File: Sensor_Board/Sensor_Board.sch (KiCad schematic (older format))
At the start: 15 parts, among them J1 Mic_Conn, U1 TLV741PxxDQNx

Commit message: Start board layout
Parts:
- removed U1: TLV741PxxDQNx, grootvoet:Texas_X2SON-4_1x1mm_P0.65mm, symbol grootvoet:TLV741PxxDQNx
- added D1: RED, LED_SMD:LED_0603_1608Metric_Pad1.05x0.95mm_HandSolder, symbol Device:LED_Small
- added R21: 2k2, Resistor_SMD:R_0603_1608Metric_Pad0.98x0.95mm_HandSolder, symbol Device:R_Small
- added U1: TLV741PxxDBVx, Package_TO_SOT_SMD:SOT-23-5, symbol grootvoet:TLV741PxxDBVx
- H1, H2: footprint MountingHole:MountingHole_2.7mm_M2.5_DIN965_Pad -> MountingHole:MountingHole_3.2mm_M3_Pad_Via
- J1: footprint Connector_PinHeader_2.54mm:PinHeader_1x08_P2.54mm_Vertical -> Connector_PinHeader_2.00mm:PinHeader_1x08_P2.00mm_Vertical
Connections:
- net +1V8: now also U1.5 (OUT)
- net +3V3: now also U1.1 (IN)
- net EN: now also U1.3 (EN)
- net GND: now also R21.2, U1.2 (GND)
- net VCC: now also D1.2 (A)
- new net: D1.1 (K), R21.1
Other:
- moved on the sheet: CB2, H1, H2, J1, R1
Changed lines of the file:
@@
 L Connector_Generic:Conn_01x08 J?
 U 1 1 5F9760C7
-P 5800 4200
+P 4650 4050
 AR Path="/5F1E182A/5F9760C7" Ref="J?"  Part="1"
 AR Path="/5EE5ECAD/5EE62C2B/5F9760C7" Ref="J?"  Part="1"
@@
 AR Path="/5F803BE9/5F9760C7" Ref="J?"  Part="1"
 AR Path="/5F9760C7" Ref="J1"  Part="1"
-F 0 "J1" H 5800 3600 50  0000 C CNN
-F 1 "Mic_Conn" H 5800 3700 50  0000 C CNN
-F 2 "Connector_PinHeader_2.54mm:PinHeader_1x08_P2.54mm_Vertical" H 5800 4200 50  0001 C CNN
-F 3 "~" H 5800 4200 50  0001 C CNN
-F 4 "" H 5800 4200 50  0001 C CNN "MPN"
-F 5 "" H 5800 4200 50  0001 C CNN "Mfr."
-	1    5800 4200
+F 0 "J1" H 4650 3450 50  0000 C CNN
+F 1 "Mic_Conn" H 4650 3550 50  0000 C CNN
+F 2 "Connector_PinHeader_2.00mm:PinHeader_1x08_P2.00mm_Vertical" H 4650 4050 50  0001 C CNN
+F 3 "~" H 4650 4050 50  0001 C CNN
+F 4 "" H 4650 4050 50  0001 C CNN "MPN"
+F 5 "" H 4650 4050 50  0001 C CNN "Mfr."
+	1    4650 4050
 	1    0    0    1
 $EndComp
@@
 L Device:R_Small R?
 U 1 1 5F976175
-P 4150 4100
+P 3750 4000
 AR Path="/5EE5ECAD/5EECE6B8/5F976175" Ref="R?"  Part="1"
 AR Path="/5EE5ECAD/5EF21991/5F976175" Ref="R?"  Part="1"
@@
 AR Path="/5F803BE9/5F976175" Ref="R?"  Part="1"
 AR Path="/5F976175" Ref="R1"  Part="1"
-F 0 "R1" H 4209 4146 50  0000 L CNN
-F 1 "100k" H 4209 4055 50  0000 L CNN
-F 2 "Resistor_SMD:R_0603_1608Metric_Pad0.98x0.95mm_HandSolder" H 4150 4100 50  0001 C CNN
-F 3 "~" H 4150 4100 50  0001 C CNN
-F 4 "RC0603FR-07100KL" H 4150 4100 50  0001 C CNN "MPN"
-F 5 "Yageo" H 4150 4100 50  0001 C CNN "Mfr."
-	1    4150 4100
+F 0 "R1" H 3809 4046 50  0000 L CNN
+F 1 "100k" H 3809 3955 50  0000 L CNN
+F 2 "Resistor_SMD:R_0603_1608Metric_Pad0.98x0.95mm_HandSolder" H 3750 4000 50  0001 C CNN
+F 3 "~" H 3750 4000 50  0001 C CNN
+F 4 "RC0603FR-07100KL" H 3750 4000 50  0001 C CNN "MPN"
+F 5 "Yageo" H 3750 4000 50  0001 C CNN "Mfr."
+	1    3750 4000
 	1    0    0    -1
 $EndComp
@@
 L Device:C_Small CB?
 U 1 1 5F976195
-P 3650 4100
+P 3250 4000
 AR Path="/5EE5ECAD/5EECE6B8/5F976195" Ref="CB?"  Part="1"
 AR Path="/5EE5ECAD/5EF21991/5F976195" Ref="CB?"  Part="1"
@@
 AR Path="/5F803BE9/5F976195" Ref="CB?"  Part="1"
 AR Path="/5F976195" Ref="CB2"  Part="1"
-F 0 "CB2" H 3742 4146 50  0000 L CNN
-F 1 "100n" H 3742 4055 50  0000 L CNN
-F 2 "Capacitor_SMD:C_0603_1608Metric_Pad1.08x0.95mm_HandSolder" H 3650 4100 50  0001 C CNN
-F 3 "~" H 3650 4100 50  0001 C CNN
-F 4 "C0603C104M5RACTU" H 3650 4100 50  0001 C CNN "MPN"
-F 5 "KEMET" H 3650 4100 50  0001 C CNN "Mfr."
-	1    3650 4100
+F 0 "CB2" H 3342 4046 50  0000 L CNN
+F 1 "100n" H 3342 3955 50  0000 L CNN
+F 2 "Capacitor_SMD:C_0603_1608Metric_Pad1.08x0.95mm_HandSolder" H 3250 4000 50  0001 C CNN
+F 3 "~" H 3250 4000 50  0001 C CNN
+F 4 "C0603C104M5RACTU" H 3250 4000 50  0001 C CNN "MPN"
+F 5 "KEMET" H 3250 4000 50  0001 C CNN "Mfr."
+	1    3250 4000
 	1    0    0    -1
 $EndComp
@@
 L Mechanical:MountingHole H?
 U 1 1 5F9761A0
-P 6500 3750
+P 6500 3800
 AR Path="/5EE5ECAD/5EECE6B8/5F9761A0" Ref="H?"  Part="1"
 AR Path="/5EE5ECAD/5EF4C631/5F9761A0" Ref="H?"  Part="1"
@@
 AR Path="/5F803BE9/5F9761A0" Ref="H?"  Part="1"
 AR Path="/5F9761A0" Ref="H2"  Part="1"
-F 0 "H2" H 6600 3796 50  0000 L CNN
-F 1 "MountingHole" H 6600 3705 50  0000 L CNN
-F 2 "MountingHole:MountingHole_2.7mm_M2.5_DIN965_Pad" H 6500 3750 50  0001 C CNN
-F 3 "~" H 6500 3750 50  0001 C CNN
-	1    6500 3750
+F 0 "H2" H 6600 3846 50  0000 L CNN
+F 1 "MountingHole" H 6600 3755 50  0000 L CNN
+F 2 "MountingHole:MountingHole_3.2mm_M3_Pad_Via" H 6500 3800 50  0001 C CNN
+F 3 "~" H 6500 3800 50  0001 C CNN
+	1    6500 3800
 	1    0    0    -1
 $EndComp
@@
 L Mechanical:MountingHole H?
 U 1 1 5F9761A6
-P 6500 3550
+P 6500 3600
 AR Path="/5EE5ECAD/5EECE6B8/5F9761A6" Ref="H?"  Part="1"
 AR Path="/5EE5ECAD/5EF4C631/5F9761A6" Ref="H?"  Part="1"
@@
 AR Path="/5F803BE9/5F9761A6" Ref="H?"  Part="1"
 AR Path="/5F9761A6" Ref="H1"  Part="1"
-F 0 "H1" H 6600 3596 50  0000 L CNN
-F 1 "MountingHole" H 6600 3505 50  0000 L CNN
-F 2 "MountingHole:MountingHole_2.7mm_M2.5_DIN965_Pad" H 6500 3550 50  0001 C CNN
-F 3 "~" H 6500 3550 50  0001 C CNN
-	1    6500 3550
+F 0 "H1" H 6600 3646 50  0000 L CNN
+F 1 "MountingHole" H 6600 3555 50  0000 L CNN
+F 2 "MountingHole:MountingHole_3.2mm_M3_Pad_Via" H 6500 3600 50  0001 C CNN
+F 3 "~" H 6500 3600 50  0001 C CNN
+	1    6500 3600
 	1    0    0    -1
 $EndComp
@@
 F 5 "KEMET" H 6300 5400 50  0001 C CNN "Mfr."
 	1    6300 5400
-	1    0    0    -1
-$EndComp
-$Comp
-L grootvoet:TLV741PxxDQNx U1
-U 1 1 5F9A84F9
-P 4250 5300
-F 0 "U1" H 4275 5665 50  0000 C CNN
-F 1 "TLV741PxxDQNx" H 4275 5574 50  0000 C CNN
-F 2 "grootvoet:Texas_X2SON-4_1x1mm_P0.65mm" H 4650 4900 50  0001 C CNN
-F 3 "" H 4650 4900 50  0001 C CNN
-F 4 "TLV74118PDQNR" H 4250 5300 50  0001 C CNN "MFN"
-F 5 "TI" H 4250 5300 50  0001 C CNN "Mfr."
-	1    4250 5300
 	1    0    0    -1
 $EndComp
@@
 Wire Wire Line
 	4250 5800 4250 5750
-Wire Wire Line
-	4250 5750 4350 5750
-Wire Wire Line
-	4250 5750 4150 5750
-Connection ~ 4250 5750
-Text GLabel 5600 3800 0    50   Input ~ 0
+Text GLabel 4450 3650 0    50   Input ~ 0
 CAL_SIG
-Text GLabel 5600 3900 0    50   Input ~ 0
+Text GLabel 4450 3750 0    50   Input ~ 0
 CAL_GND
-Text GLabel 5600 4000 0    50   Input ~ 0
+Text GLabel 4450 3850 0    50   Input ~ 0
 CAL_EN
-Text GLabel 5600 4100 0    50   Input ~ 0
+Text GLabel 4450 3950 0    50   Input ~ 0
 EN
-Text GLabel 5600 4400 0    50   Input ~ 0
+Text GLabel 4450 4250 0    50   Input ~ 0
 SIG_P
-Text GLabel 5600 4500 0    50   Input ~ 0
+Text GLabel 4450 4350 0    50   Input ~ 0
 SIG_N
 $Comp
 L power:VCC #PWR09
 U 1 1 5FA24F87
-P 5600 4200
-F 0 "#PWR09" H 5600 4050 50  0001 C CNN
-F 1 "VCC" V 5615 4327 50  0000 L CNN
-F 2 "" H 5600 4200 50  0001 C CNN
-F 3 "" H 5600 4200 50  0001 C CNN
-	1    5600 4200
+P 4450 4050
+F 0 "#PWR09" H 4450 3900 50  0001 C CNN
+F 1 "VCC" V 4465 4177 50  0000 L CNN
+F 2 "" H 4450 4050 50  0001 C CNN
+F 3 "" H 4450 4050 50  0001 C CNN
+	1    4450 4050
 	0    -1   -1   0
 $EndComp
@@
 L power:GND #PWR010
 U 1 1 5FA257DC
-P 5600 4300
-F 0 "#PWR010" H 5600 4050 50  0001 C CNN
-F 1 "GND" V 5605 4172 50  0000 R CNN
-F 2 "" H 5600 4300 50  0001 C CNN
-F 3 "" H 5600 4300 50  0001 C CNN
-	1    5600 4300
+P 4450 4150
+F 0 "#PWR010" H 4450 3900 50  0001 C CNN
+F 1 "GND" V 4455 4022 50  0000 R CNN
+F 2 "" H 4450 4150 50  0001 C CNN
+F 3 "" H 4450 4150 50  0001 C CNN
+	1    4450 4150
 	0    1    1    0
 $EndComp
@@
 L power:GND #PWR03
 U 1 1 5FA272C8
-P 3650 4200
-F 0 "#PWR03" H 3650 3950 50  0001 C CNN
-F 1 "GND" H 3655 4027 50  0000 C CNN
-F 2 "" H 3650 4200 50  0001 C CNN
-F 3 "" H 3650 4200 50  0001 C CNN
-	1    3650 4200
-	1    0    0    -1
-$EndComp
-Text GLabel 3650 4000 1    50   Input ~ 0
+P 3250 4100
+F 0 "#PWR03" H 3250 3850 50  0001 C CNN
+F 1 "GND" H 3255 3927 50  0000 C CNN
+F 2 "" H 3250 4100 50  0001 C CNN
+F 3 "" H 3250 4100 50  0001 C CNN
+	1    3250 4100
+	1    0    0    -1
+$EndComp
+Text GLabel 3250 3900 1    50   Input ~ 0
 EN
-Text GLabel 4150 4200 3    50   Input ~ 0
+Text GLabel 3750 4100 3    50   Input ~ 0
 EN
 $Comp
@@
 L power:VCC #PWR04
 U 1 1 5FA6370F
-P 4150 4000
-F 0 "#PWR04" H 4150 3850 50  0001 C CNN
-F 1 "VCC" H 4165 4173 50  0000 C CNN
-F 2 "" H 4150 4000 50  0001 C CNN
-F 3 "" H 4150 4000 50  0001 C CNN
-	1    4150 4000
+P 3750 3900
+F 0 "#PWR04" H 3750 3750 50  0001 C CNN
+F 1 "VCC" H 3765 4073 50  0000 C CNN
+F 2 "" H 3750 3900 50  0001 C CNN
+F 3 "" H 3750 3900 50  0001 C CNN
+	1    3750 3900
 	1    0    0    -1
 $EndComp
@@
 Text Notes 3050 1650 0    50   ~ 10
 Signal Chain
-NoConn ~ 5600 4000
-NoConn ~ 5600 3900
-NoConn ~ 5600 3800
+NoConn ~ 4450 3850
+NoConn ~ 4450 3750
+NoConn ~ 4450 3650
 $Comp
 L power:+3V3 #PWR01
@@
 Wire Wire Line
 	5350 2450 5000 2450
+$Comp
+L grootvoet:TLV741PxxDBVx U1
+U 1 1 5F90B83C
+P 4250 5300
+F 0 "U1" H 4300 5665 50  0000 C CNN
+F 1 "TLV741PxxDBVx" H 4300 5574 50  0000 C CNN
+F 2 "Package_TO_SOT_SMD:SOT-23-5" H 4650 4900 50  0001 C CNN
+F 3 "" H 4650 4900 50  0001 C CNN
+	1    4250 5300
+	1    0    0    -1
+$EndComp
+$Comp
+L Device:LED_Small D1
+U 1 1 5F915892
+P 5250 3900
+F 0 "D1" V 5296 3830 50  0000 R CNN
+F 1 "RED" V 5205 3830 50  0000 R CNN
+F 2 "LED_SMD:LED_0603_1608Metric_Pad1.05x0.95mm_HandSolder" V 5250 3900 50  0001 C CNN
+F 3 "~" V 5250 3900 50  0001 C CNN
+	1    5250 3900
+	0    -1   -1   0
+$EndComp
+$Comp
+L Device:R_Small R?
+U 1 1 5F915C70
+P 5250 4100
+AR Path="/5EE5ECAD/5EECE6B8/5F915C70" Ref="R?"  Part="1"
+AR Path="/5EE5ECAD/5EF21991/5F915C70" Ref="R?"  Part="1"
+AR Path="/5EE5ECAD/5EF33EA2/5F915C70" Ref="R?"  Part="1"
+AR Path="/5EE5ECAD/5EF4C631/5F915C70" Ref="R?"  Part="1"
+AR Path="/5EE5ECAD/5F0013E5/5F915C70" Ref="R?"  Part="1"
+AR Path="/5EE5ECAD/5F0090C7/5F915C70" Ref="R?"  Part="1"
+AR Path="/5F803BE9/5F915C70" Ref="R?"  Part="1"
+AR Path="/5F915C70" Ref="R21"  Part="1"
+F 0 "R21" H 5309 4146 50  0000 L CNN
+F 1 "2k2" H 5309 4055 50  0000 L CNN
+F 2 "Resistor_SMD:R_0603_1608Metric_Pad0.98x0.95mm_HandSolder" H 5250 4100 50  0001 C CNN
+F 3 "~" H 5250 4100 50  0001 C CNN
+F 4 "" H 5250 4100 50  0001 C CNN "MPN"
+F 5 "Yageo" H 5250 4100 50  0001 C CNN "Mfr."
+	1    5250 4100
+	1    0    0    -1
+$EndComp
+$Comp
+L power:GND #PWR064
+U 1 1 5F91626C
+P 5250 4200
+F 0 "#PWR064" H 5250 3950 50  0001 C CNN
+F 1 "GND" H 5255 4027 50  0000 C CNN
+F 2 "" H 5250 4200 50  0001 C CNN
+F 3 "" H 5250 4200 50  0001 C CNN
+	1    5250 4200
+	1    0    0    -1
+$EndComp
+$Comp
+L power:VCC #PWR063
+U 1 1 5F9167F7
+P 5250 3800
+F 0 "#PWR063" H 5250 3650 50  0001 C CNN
+F 1 "VCC" V 5265 3927 50  0000 L CNN
+F 2 "" H 5250 3800 50  0001 C CNN
+F 3 "" H 5250 3800 50  0001 C CNN
+	1    5250 3800
+	1    0    0    -1
+$EndComp
 $EndSCHEMATC

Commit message: Add connector
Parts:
- J1: footprint Connector_PinHeader_2.00mm:PinHeader_1x08_P2.00mm_Vertical -> grootvoet:TE_7-215079-8; MPN (none) -> 7-215079-8, 7-215083-8; Mfr. (none) -> TE Connectivity
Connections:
- net CAL_EN is gone; now on net VCC: J1.6 (Pin_6)
- net EN: now also J1.4 (Pin_4); no longer J1.5 (Pin_5)
- net GND: now also J1.5 (Pin_5)
- net SIG_N: now also J1.2 (Pin_2); no longer J1.1 (Pin_1)
- net SIG_P: now also J1.1 (Pin_1); no longer J1.2 (Pin_2)
- net VCC: no longer J1.4 (Pin_4)
- net CAL_GND: no longer names the net of J1.7 (Pin_7)
- net CAL_SIG: no longer names the net of J1.8 (Pin_8)
- no-connect marks 3 -> 2
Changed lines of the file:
@@
 Comment4 "CM Geldenhuys"
 $EndDescr
-$Comp
-L Connector_Generic:Conn_01x08 J?
-U 1 1 5F9760C7
-P 4650 4050
-AR Path="/5F1E182A/5F9760C7" Ref="J?"  Part="1"
-AR Path="/5EE5ECAD/5EE62C2B/5F9760C7" Ref="J?"  Part="1"
-AR Path="/5EE5ECAD/5EE62C39/5F9760C7" Ref="J?"  Part="1"
-AR Path="/5EE5ECAD/5EE62C47/5F9760C7" Ref="J?"  Part="1"
-AR Path="/5EE5ECAD/5EE62C55/5F9760C7" Ref="J?"  Part="1"
-AR Path="/5EE5ECAD/5EE8F49C/5F9760C7" Ref="J?"  Part="1"
-AR Path="/5EE5ECAD/5EE91C9A/5F9760C7" Ref="J?"  Part="1"
-AR Path="/5EE5ECAD/5EE94935/5F9760C7" Ref="J?"  Part="1"
-AR Path="/5EE1D522/5F9760C7" Ref="J?"  Part="1"
-AR Path="/5EE5ECAD/5EECE6B8/5F9760C7" Ref="J?"  Part="1"
-AR Path="/5EE5ECAD/5EF21991/5F9760C7" Ref="J?"  Part="1"
-AR Path="/5EE5ECAD/5EF33EA2/5F9760C7" Ref="J?"  Part="1"
-AR Path="/5EE5ECAD/5EF4C631/5F9760C7" Ref="J?"  Part="1"
-AR Path="/5EE5ECAD/5F0013E5/5F9760C7" Ref="J?"  Part="1"
-AR Path="/5EE5ECAD/5F0090C7/5F9760C7" Ref="J?"  Part="1"
-AR Path="/5F803BE9/5F9760C7" Ref="J?"  Part="1"
-AR Path="/5F9760C7" Ref="J1"  Part="1"
-F 0 "J1" H 4650 3450 50  0000 C CNN
-F 1 "Mic_Conn" H 4650 3550 50  0000 C CNN
-F 2 "Connector_PinHeader_2.00mm:PinHeader_1x08_P2.00mm_Vertical" H 4650 4050 50  0001 C CNN
-F 3 "~" H 4650 4050 50  0001 C CNN
-F 4 "" H 4650 4050 50  0001 C CNN "MPN"
-F 5 "" H 4650 4050 50  0001 C CNN "Mfr."
-	1    4650 4050
-	1    0    0    1
-$EndComp
 Text Notes 3050 4800 0    50   ~ 10
 Power Supply Filtering and Resivoir
@@
 Wire Wire Line
 	4250 5800 4250 5750
-Text GLabel 4450 3650 0    50   Input ~ 0
-CAL_SIG
-Text GLabel 4450 3750 0    50   Input ~ 0
-CAL_GND
-Text GLabel 4450 3850 0    50   Input ~ 0
-CAL_EN
-Text GLabel 4450 3950 0    50   Input ~ 0
+Text GLabel 4450 4050 0    50   Input ~ 0
 EN
-Text GLabel 4450 4250 0    50   Input ~ 0
-SIG_P
-Text GLabel 4450 4350 0    50   Input ~ 0
-SIG_N
 $Comp
 L power:VCC #PWR09
 U 1 1 5FA24F87
-P 4450 4050
-F 0 "#PWR09" H 4450 3900 50  0001 C CNN
-F 1 "VCC" V 4465 4177 50  0000 L CNN
-F 2 "" H 4450 4050 50  0001 C CNN
-F 3 "" H 4450 4050 50  0001 C CNN
-	1    4450 4050
+P 4450 3850
+F 0 "#PWR09" H 4450 3700 50  0001 C CNN
+F 1 "VCC" V 4465 3977 50  0000 L CNN
+F 2 "" H 4450 3850 50  0001 C CNN
+F 3 "" H 4450 3850 50  0001 C CNN
+	1    4450 3850
 	0    -1   -1   0
 $EndComp
@@
 Text Notes 3050 1650 0    50   ~ 10
 Signal Chain
-NoConn ~ 4450 3850
 NoConn ~ 4450 3750
 NoConn ~ 4450 3650
@@
 	1    0    0    -1
 $EndComp
+$Comp
+L Connector_Generic:Conn_01x08 J?
+U 1 1 5F9760C7
+P 4650 4050
+AR Path="/5F1E182A/5F9760C7" Ref="J?"  Part="1"
+AR Path="/5EE5ECAD/5EE62C2B/5F9760C7" Ref="J?"  Part="1"
+AR Path="/5EE5ECAD/5EE62C39/5F9760C7" Ref="J?"  Part="1"
+AR Path="/5EE5ECAD/5EE62C47/5F9760C7" Ref="J?"  Part="1"
+AR Path="/5EE5ECAD/5EE62C55/5F9760C7" Ref="J?"  Part="1"
+AR Path="/5EE5ECAD/5EE8F49C/5F9760C7" Ref="J?"  Part="1"
+AR Path="/5EE5ECAD/5EE91C9A/5F9760C7" Ref="J?"  Part="1"
+AR Path="/5EE5ECAD/5EE94935/5F9760C7" Ref="J?"  Part="1"
+AR Path="/5EE1D522/5F9760C7" Ref="J?"  Part="1"
+AR Path="/5EE5ECAD/5EECE6B8/5F9760C7" Ref="J?"  Part="1"
+AR Path="/5EE5ECAD/5EF21991/5F9760C7" Ref="J?"  Part="1"
+AR Path="/5EE5ECAD/5EF33EA2/5F9760C7" Ref="J?"  Part="1"
+AR Path="/5EE5ECAD/5EF4C631/5F9760C7" Ref="J?"  Part="1"
+AR Path="/5EE5ECAD/5F0013E5/5F9760C7" Ref="J?"  Part="1"
+AR Path="/5EE5ECAD/5F0090C7/5F9760C7" Ref="J?"  Part="1"
+AR Path="/5F803BE9/5F9760C7" Ref="J?"  Part="1"
+AR Path="/5F9760C7" Ref="J1"  Part="1"
+F 0 "J1" H 4650 3450 50  0000 C CNN
+F 1 "Mic_Conn" H 4650 3550 50  0000 C CNN
+F 2 "grootvoet:TE_7-215079-8" H 4650 4050 50  0001 C CNN
+F 3 "~" H 4650 4050 50  0001 C CNN
+F 4 "7-215079-8, 7-215083-8" H 4650 4050 50  0001 C CNN "MPN"
+F 5 "TE Connectivity" H 4650 4050 50  0001 C CNN "Mfr."
+	1    4650 4050
+	1    0    0    1
+$EndComp
+$Comp
+L power:GND #PWR0101
+U 1 1 5F8DD1D1
+P 4450 3950
+F 0 "#PWR0101" H 4450 3700 50  0001 C CNN
+F 1 "GND" V 4455 3822 50  0000 R CNN
+F 2 "" H 4450 3950 50  0001 C CNN
+F 3 "" H 4450 3950 50  0001 C CNN
+	1    4450 3950
+	0    1    1    0
+$EndComp
+Text GLabel 4450 4350 0    50   Input ~ 0
+SIG_P
+Text GLabel 4450 4250 0    50   Input ~ 0
+SIG_N
 $EndSCHEMATC

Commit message: Update Footprint & part num.
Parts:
- C2: footprint Capacitor_SMD:C_0603_1608Metric_Pad1.08x0.95mm_HandSolder -> Capacitor_SMD:C_0805_2012Metric_Pad1.18x1.45mm_HandSolder
- D1: MPN (none) -> SML-D12U8WT86C; Mfr. (none) -> ROHM Semiconductor
- R21: Mfr. Yageo -> Panasonic
- TP1: Mfr. (none) -> Panasonic
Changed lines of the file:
@@
 F 2 "TestPoint:TestPoint_Pad_D1.0mm" H 6800 5200 50  0001 C CNN
 F 3 "~" H 6800 5200 50  0001 C CNN
+F 4 "Panasonic" H 6600 5200 50  0001 C CNN "Mfr."
 	1    6600 5200
 	1    0    0    -1
@@
 F 0 "C2" H 6392 5446 50  0000 L CNN
 F 1 "10u" H 6392 5355 50  0000 L CNN
-F 2 "Capacitor_SMD:C_0603_1608Metric_Pad1.08x0.95mm_HandSolder" H 6300 5400 50  0001 C CNN
+F 2 "Capacitor_SMD:C_0805_2012Metric_Pad1.18x1.45mm_HandSolder" H 6300 5400 50  0001 C CNN
 F 3 "~" H 6300 5400 50  0001 C CNN
 F 4 "C0805C106K9PACTU" H 6300 5400 50  0001 C CNN "MPN"
@@
 F 2 "LED_SMD:LED_0603_1608Metric_Pad1.05x0.95mm_HandSolder" V 5250 3900 50  0001 C CNN
 F 3 "~" V 5250 3900 50  0001 C CNN
+F 4 "SML-D12U8WT86C" H 5250 3900 50  0001 C CNN "MPN"
+F 5 "ROHM Semiconductor" H 5250 3900 50  0001 C CNN "Mfr."
 	1    5250 3900
 	0    -1   -1   0
@@
 F 3 "~" H 5250 4100 50  0001 C CNN
 F 4 "" H 5250 4100 50  0001 C CNN "MPN"
-F 5 "Yageo" H 5250 4100 50  0001 C CNN "Mfr."
+F 5 "Panasonic" H 5250 4100 50  0001 C CNN "Mfr."
 	1    5250 4100
 	1    0    0    -1

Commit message: Update BOM
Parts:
- R21: MPN (none) -> ERJ-3EKF2201V
- TP1: MPN (none) -> ICS-40300; Mfr. Panasonic -> TDK InvenSense
- U1: MPN (none) -> TLV74118PDBVR; Mfr. (none) -> Texas Instruments
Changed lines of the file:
@@
 F 2 "TestPoint:TestPoint_Pad_D1.0mm" H 6800 5200 50  0001 C CNN
 F 3 "~" H 6800 5200 50  0001 C CNN
-F 4 "Panasonic" H 6600 5200 50  0001 C CNN "Mfr."
+F 4 "TDK InvenSense" H 6600 5200 50  0001 C CNN "Mfr."
+F 5 "ICS-40300" H 6600 5200 50  0001 C CNN "MPN"
 	1    6600 5200
 	1    0    0    -1
@@
 F 2 "Package_TO_SOT_SMD:SOT-23-5" H 4650 4900 50  0001 C CNN
 F 3 "" H 4650 4900 50  0001 C CNN
+F 4 "TLV74118PDBVR" H 4250 5300 50  0001 C CNN "MPN"
+F 5 "Texas Instruments" H 4250 5300 50  0001 C CNN "Mfr."
 	1    4250 5300
 	1    0    0    -1
@@
 F 2 "Resistor_SMD:R_0603_1608Metric_Pad0.98x0.95mm_HandSolder" H 5250 4100 50  0001 C CNN
 F 3 "~" H 5250 4100 50  0001 C CNN
-F 4 "" H 5250 4100 50  0001 C CNN "MPN"
+F 4 "ERJ-3EKF2201V" H 5250 4100 50  0001 C CNN "MPN"
 F 5 "Panasonic" H 5250 4100 50  0001 C CNN "Mfr."
 	1    5250 4100

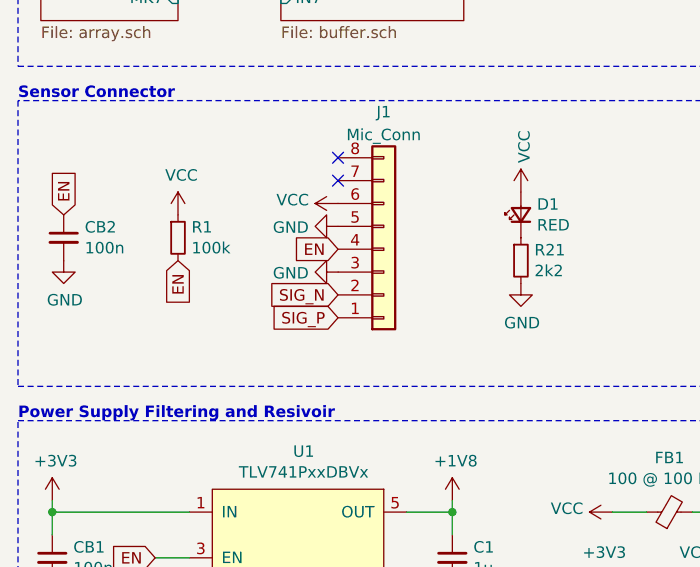
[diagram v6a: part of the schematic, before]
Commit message: New ADC board layout
Merge feature/kv-new-adc

Squashed commit of the following:
===============================================

commit d560af3129baffdc71a13a7fa7beda6d7e4b1bbe
Author: CM Geldenhuys <20198329@sun.ac.za>
Date:   Mon Nov 2 10:16:05 2020 +0200

    Change board layout

commit e0e102b1b715915958904bd07514080422fcc802
Author: CM Geldenhuys <20198329@sun.ac.za>
Date:   Mon Nov 2 08:42:49 2020 +0200

    Route ADC rst

commit dbc5adba55d665b163eedfb4150514fe2b5b8ec8
Author: CM Geldenhuys <20198329@sun.ac.za>
Date:   Mon Nov 2 08:37:27 2020 +0200

    Fix GPS conn.

commit 0f139c20ac4bbbbfd2ab5507f187a5ddf70be7a1
Author: CM Geldenhuys <20198329@sun.ac.za>
Date:   Mon Nov 2 08:23:01 2020 +0200

    Route USR BTN

commit f6bd16c8e79a9fc3047a82e3e1abb388a579a1e4
Author: CM Geldenhuys <20198329@sun.ac.za>
Date:   Sun Nov 1 07:41:20 2020 +0200

    Route GPS Conn

commit 016e6e7ba1ce602e3233b00102ced6621a380f78
Author: CM Geldenhuys <20198329@sun.ac.za>
Date:   Fri Oct 30 17:31:13 2020 +0200

    Route Misc.

commit 6a809ae2e129821f12cca4ec3806ebf69337c268
Author: CM Geldenhuys <20198329@sun.ac.za>
Date:   Fri Oct 30 11:40:29 2020 +0200

    (WIP) SD config

commit b5d79f248cd283a71c5ab746a4afc4eb96850216
Author: CM Geldenhuys <20198329@sun.ac.za>
Date:   Fri Oct 30 11:24:56 2020 +0200

    Route ST-Link

commit dba35a7554c0c60ddd581dd4b7cbdf28445f26a1
Author: CM Geldenhuys <20198329@sun.ac.za>
Date:   Fri Oct 30 11:03:44 2020 +0200

    Route out GND planes

commit ee78e0f947a8edc358d3e2ec17c7ddf8f87e82dd
Author: CM Geldenhuys <20198329@sun.ac.za>
Date:   Thu Oct 29 16:17:03 2020 +0200

    Change ST-LINk loc.

commit b281a3fe16ed9d80db1964422c72eaf6acbfd9f3
Author: CM Geldenhuys <20198329@sun.ac.za>
Date:   Thu Oct 29 15:43:37 2020 +0200

    Major layout update

commit 655eae6cd0c7e79d683f16c4706ab989a6952fc5
Author: CM Geldenhuys <20198329@sun.ac.za>
Date:   Thu Oct 29 12:05:26 2020 +0200

    Route analog section

commit 0aa4140e89fcb36b0e9f339e25cad0a47a5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
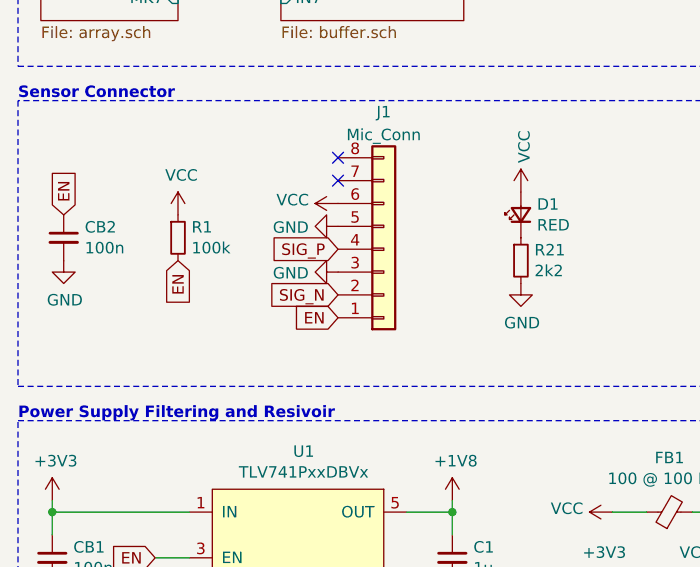
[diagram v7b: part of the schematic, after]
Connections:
- net EN: now also J1.1 (Pin_1); no longer J1.4 (Pin_4)
- net SIG_P: now also J1.4 (Pin_4); no longer J1.1 (Pin_1)
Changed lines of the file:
@@
 Wire Wire Line
 	4250 5800 4250 5750
-Text GLabel 4450 4050 0    50   Input ~ 0
+Text GLabel 4450 4350 0    50   Input ~ 0
 EN
 $Comp
@@
 	0    1    1    0
 $EndComp
-Text GLabel 4450 4350 0    50   Input ~ 0
+Text GLabel 4450 4050 0    50   Input ~ 0
 SIG_P
 Text GLabel 4450 4250 0    50   Input ~ 0

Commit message: Update connector
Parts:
- removed CB2: 100n, Capacitor_SMD:C_0603_1608Metric_Pad1.08x0.95mm_HandSolder, symbol Device:C_Small
- J1: symbol Connector_Generic:Conn_01x08 -> Connector_Generic:Conn_02x04_Odd_Even
- R1: value 100k -> 10k; MPN RC0603FR-07100KL -> (none)
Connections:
- net +3V3: now also R1.1
- net GND: now also J1.2 (Pin_2), J1.4 (Pin_4), J1.6 (Pin_6), J1.8 (Pin_8); no longer J1.3 (Pin_3), J1.5 (Pin_5)
- net SIG_N: now also J1.3 (Pin_3); no longer J1.2 (Pin_2)
- net SIG_P: now also J1.5 (Pin_5); no longer J1.4 (Pin_4)
- net VCC: now also J1.7 (Pin_7); no longer J1.6 (Pin_6), R1.1
- net EN: no longer names the net of R1.2, U1.3 (EN)
- net EN: no longer J1.1 (Pin_1)
- no-connect marks 2 -> 1
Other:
- moved on the sheet: C2, FB1, J1, R1, TP1
